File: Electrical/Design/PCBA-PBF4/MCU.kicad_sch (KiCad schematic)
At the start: 57 parts, among them J701 Conn_Coaxial, J702 (NF), J799 Conn_01x02, SW701 C255807, SW702 C2905169, SW703 C2905169, U703 RP2040, U704 ESP32-S3FN8, U705 W25Q64JVSSIQ, Y701 ESP32_XTAL

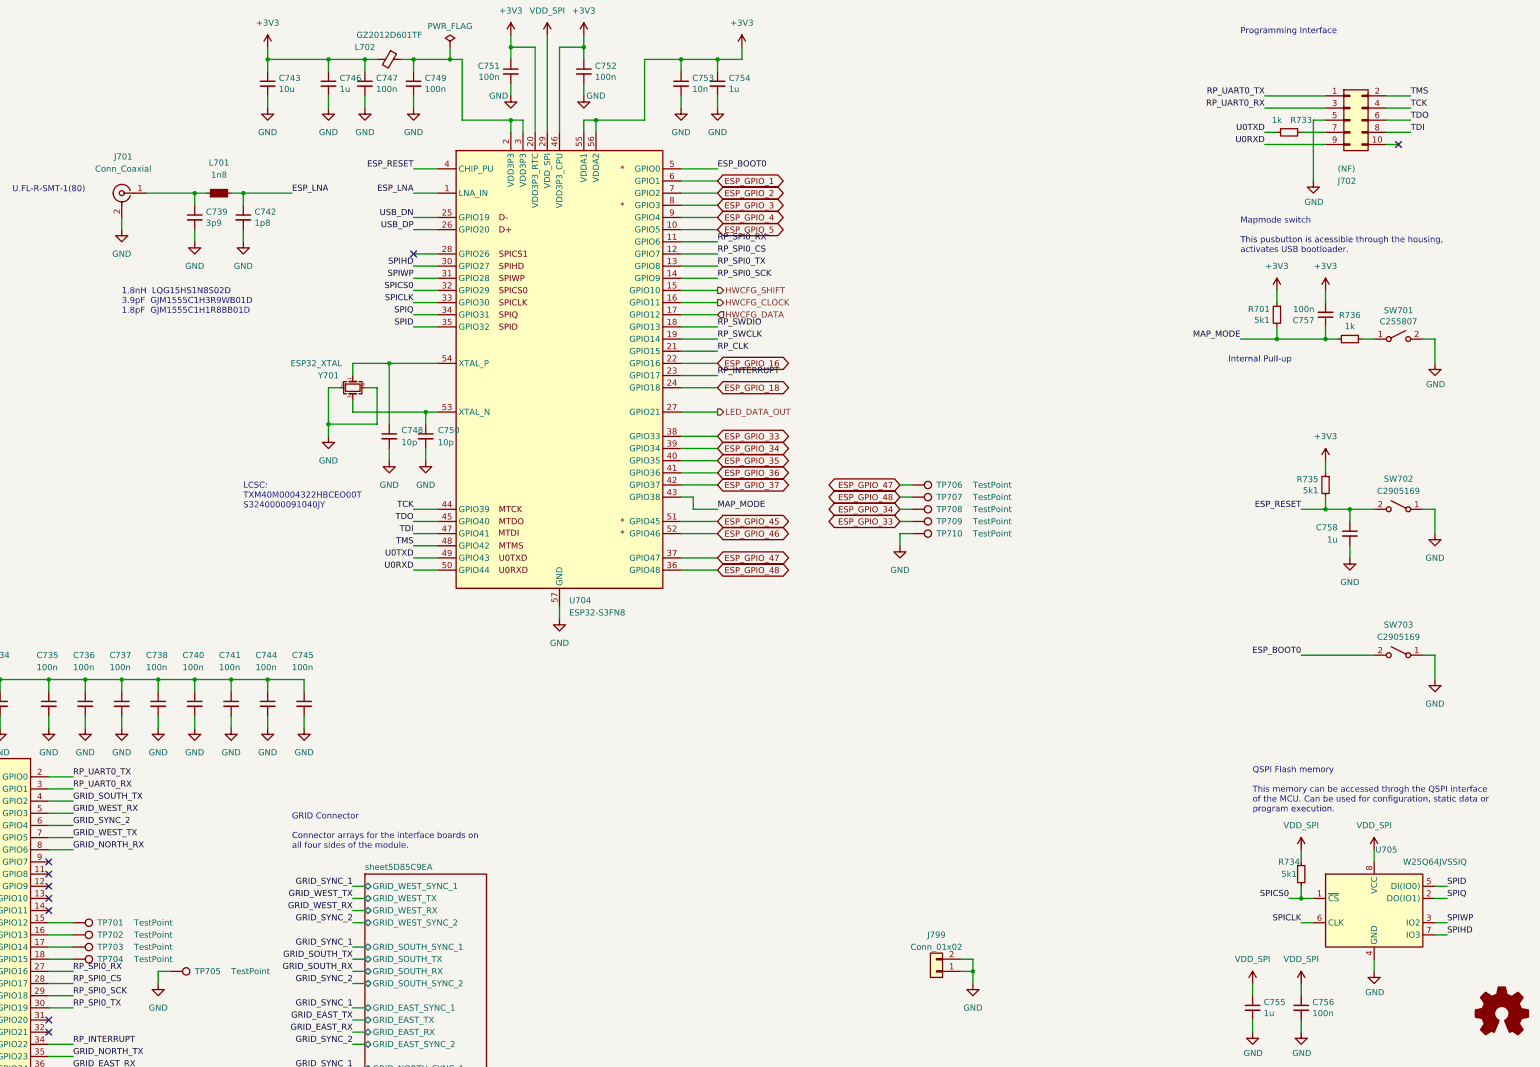
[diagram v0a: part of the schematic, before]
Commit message: SUKU pcbs updated with footprint and symbol values
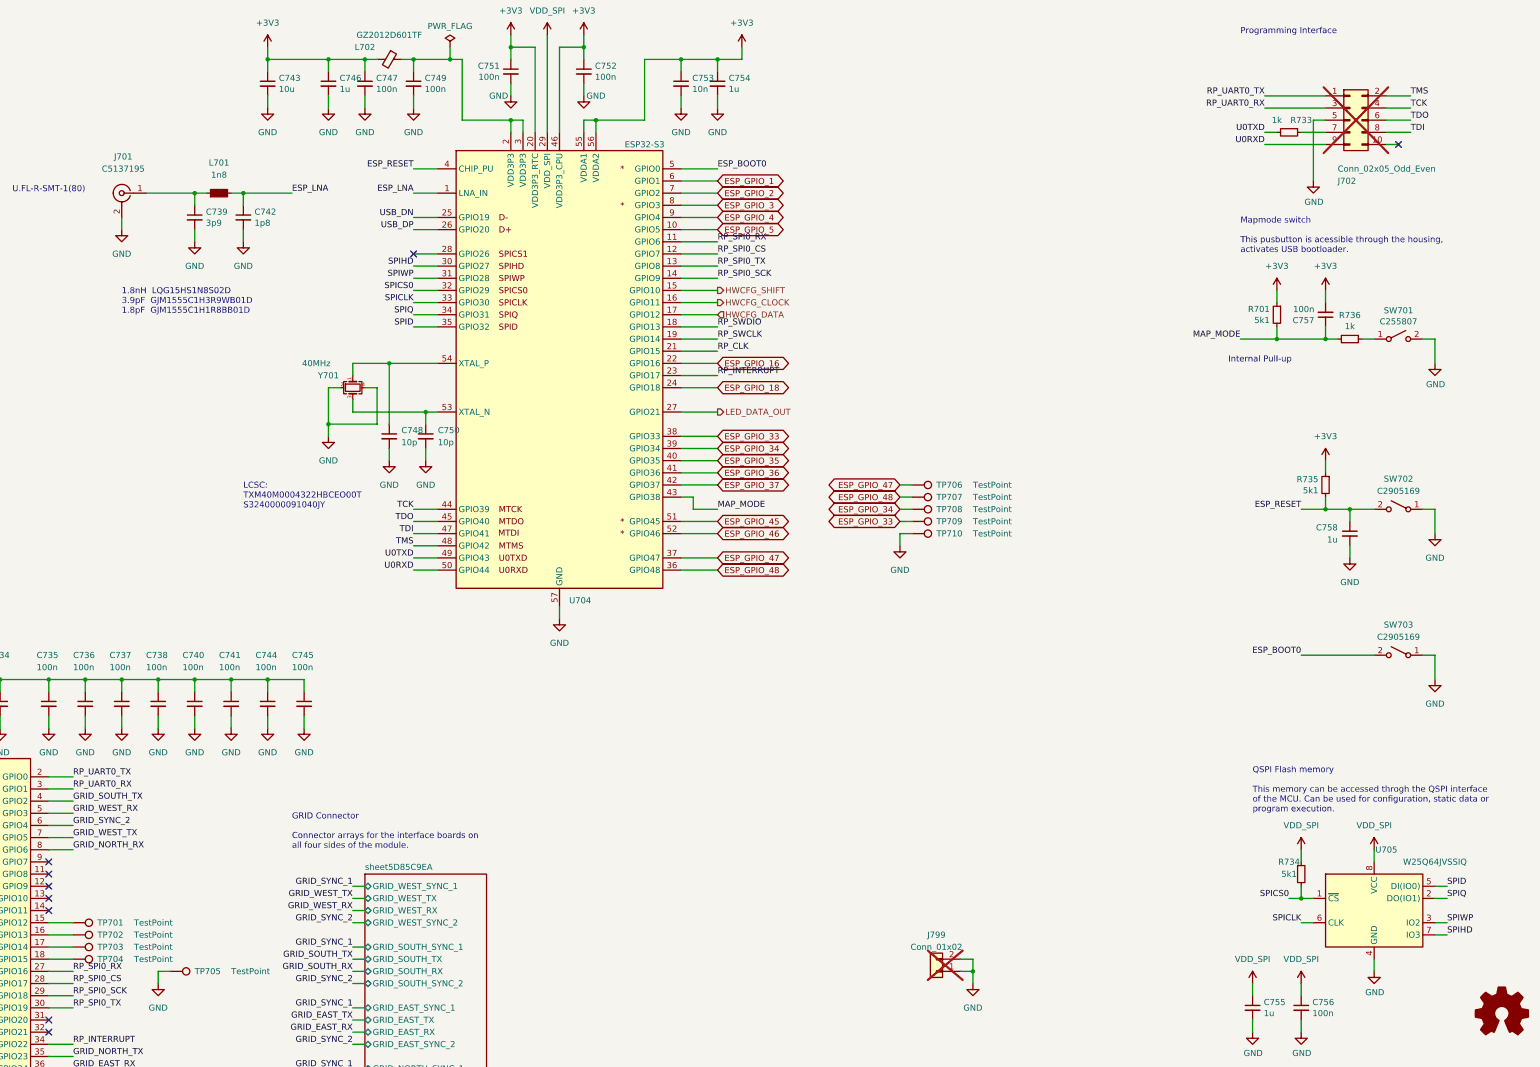
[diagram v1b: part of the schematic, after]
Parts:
- J701: value Conn_Coaxial -> C5137195
- J702: value (NF) -> Conn_02x05_Odd_Even; now not fitted; now left out of the parts list
- J799: now not fitted; now left out of the parts list
- U704: value ESP32-S3FN8 -> ESP32-S3; symbol suku_basics:ESP32-S3FN8 -> suku_basics:ESP32-S3
- Y701: value ESP32_XTAL -> 40MHz

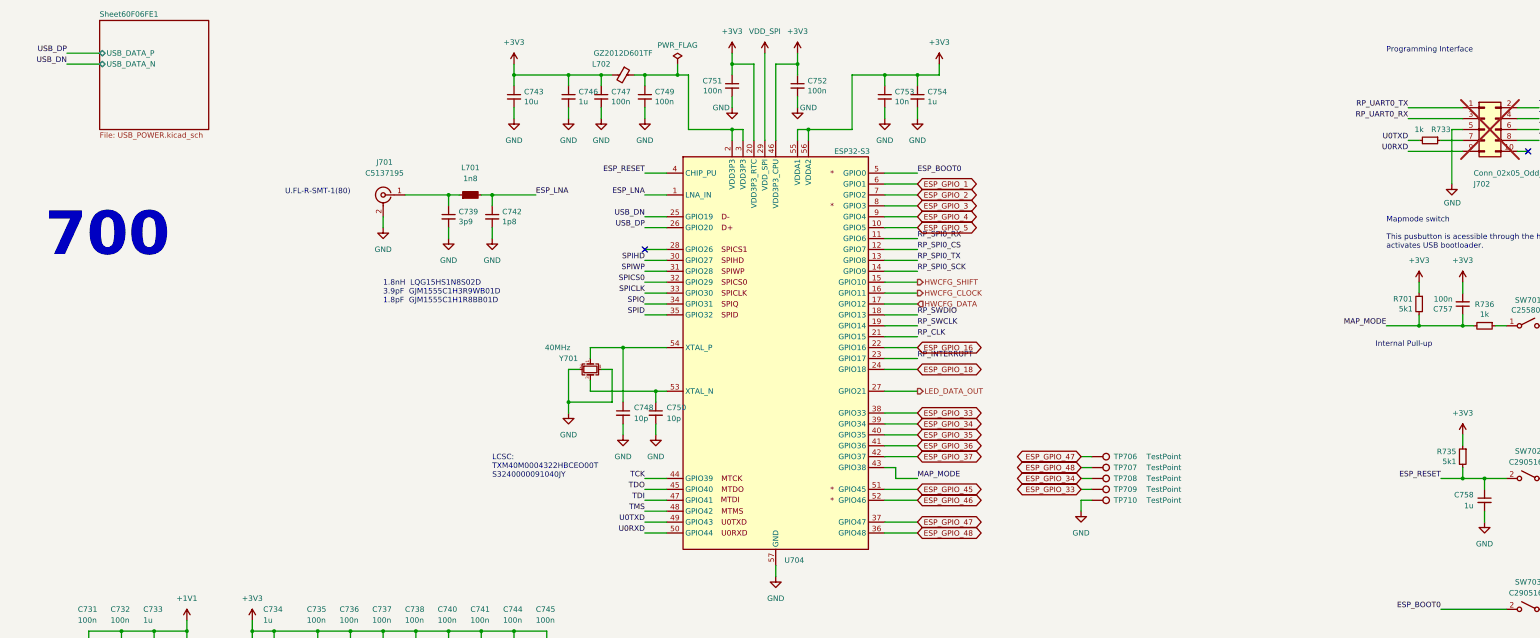
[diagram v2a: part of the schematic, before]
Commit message: SUKU debug adapter support added to PBF4
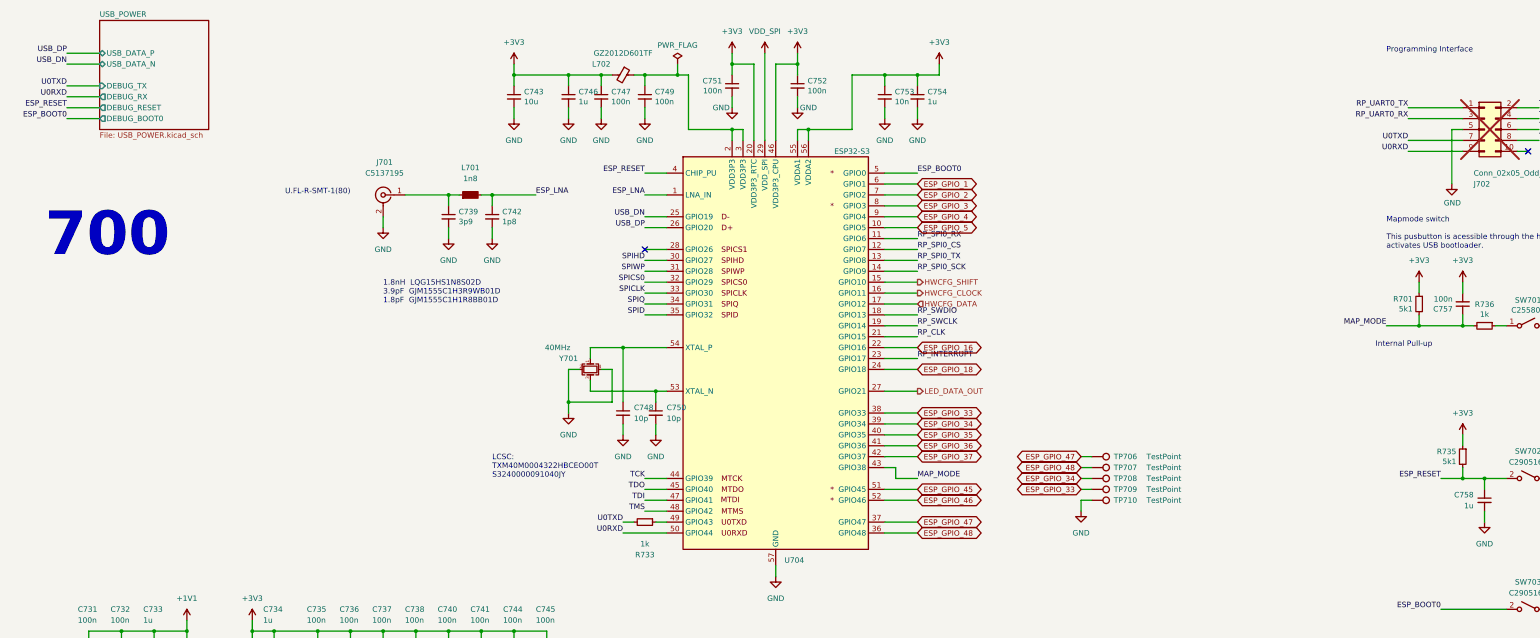
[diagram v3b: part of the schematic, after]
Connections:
- net U0TXD: now also J702.7 (Pin_7); no longer U704.49 (GPIO43)
- net at R733.1: now also U704.49 (GPIO43); no longer J702.7 (Pin_7)
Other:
- removed sheet Sheet60F06FE1
- added sheet USB_POWER (USB_POWER.kicad_sch)
- moved on the sheet: R733

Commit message: SUKU reset and boot button footprints updated
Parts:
- SW702, SW703: footprint Button_Switch_SMD:SW_SPST_CK_RS282G05A3 -> suku_basics:SW_SPST_CK_RS282G05A3
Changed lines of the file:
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@@
 			)
 		)
-		(property "Footprint" "Button_Switch_SMD:SW_SPST_CK_RS282G05A3"
+		(property "Footprint" "suku_basics:SW_SPST_CK_RS282G05A3"
 			(at 370.84 132.08 0)
 			(effects
@@
 			)
 		)
-		(property "Footprint" "Button_Switch_SMD:SW_SPST_CK_RS282G05A3"
+		(property "Footprint" "suku_basics:SW_SPST_CK_RS282G05A3"
 			(at 370.84 162.56 0)
 			(effects
